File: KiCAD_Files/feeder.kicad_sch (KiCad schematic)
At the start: 8 parts

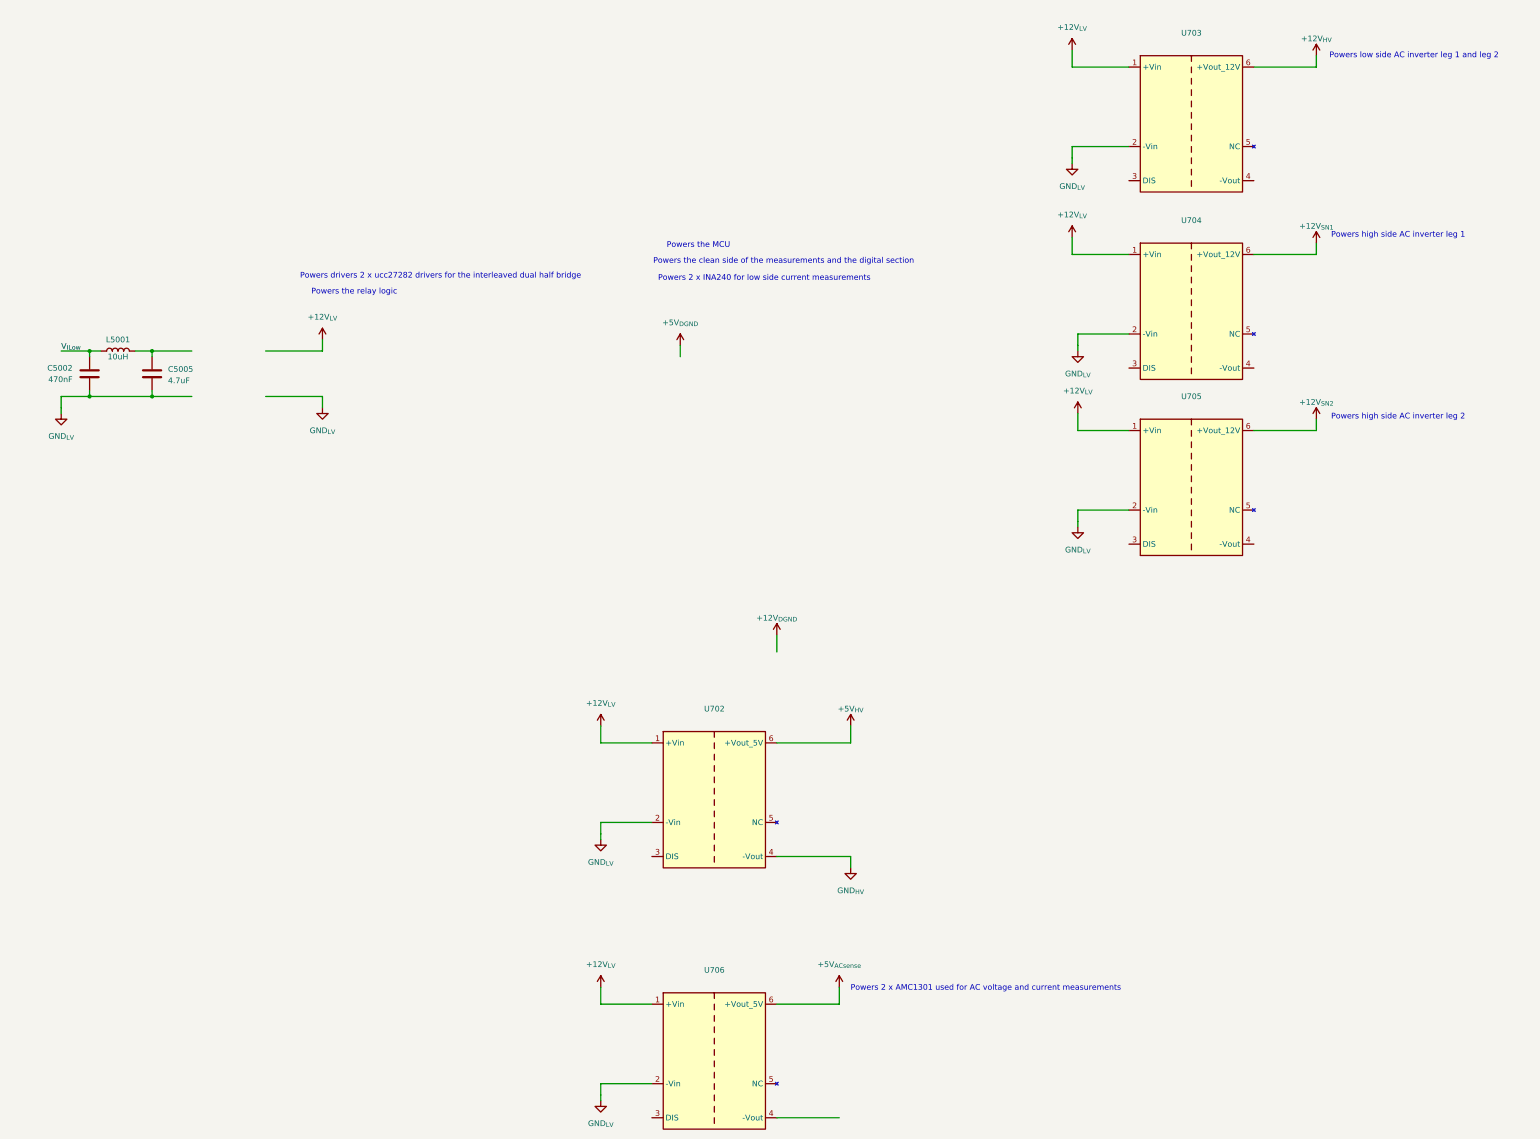
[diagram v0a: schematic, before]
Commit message: First routing pass complete.
Signed-off-by: Jean Alinei <jean.alinei@owntech.org>
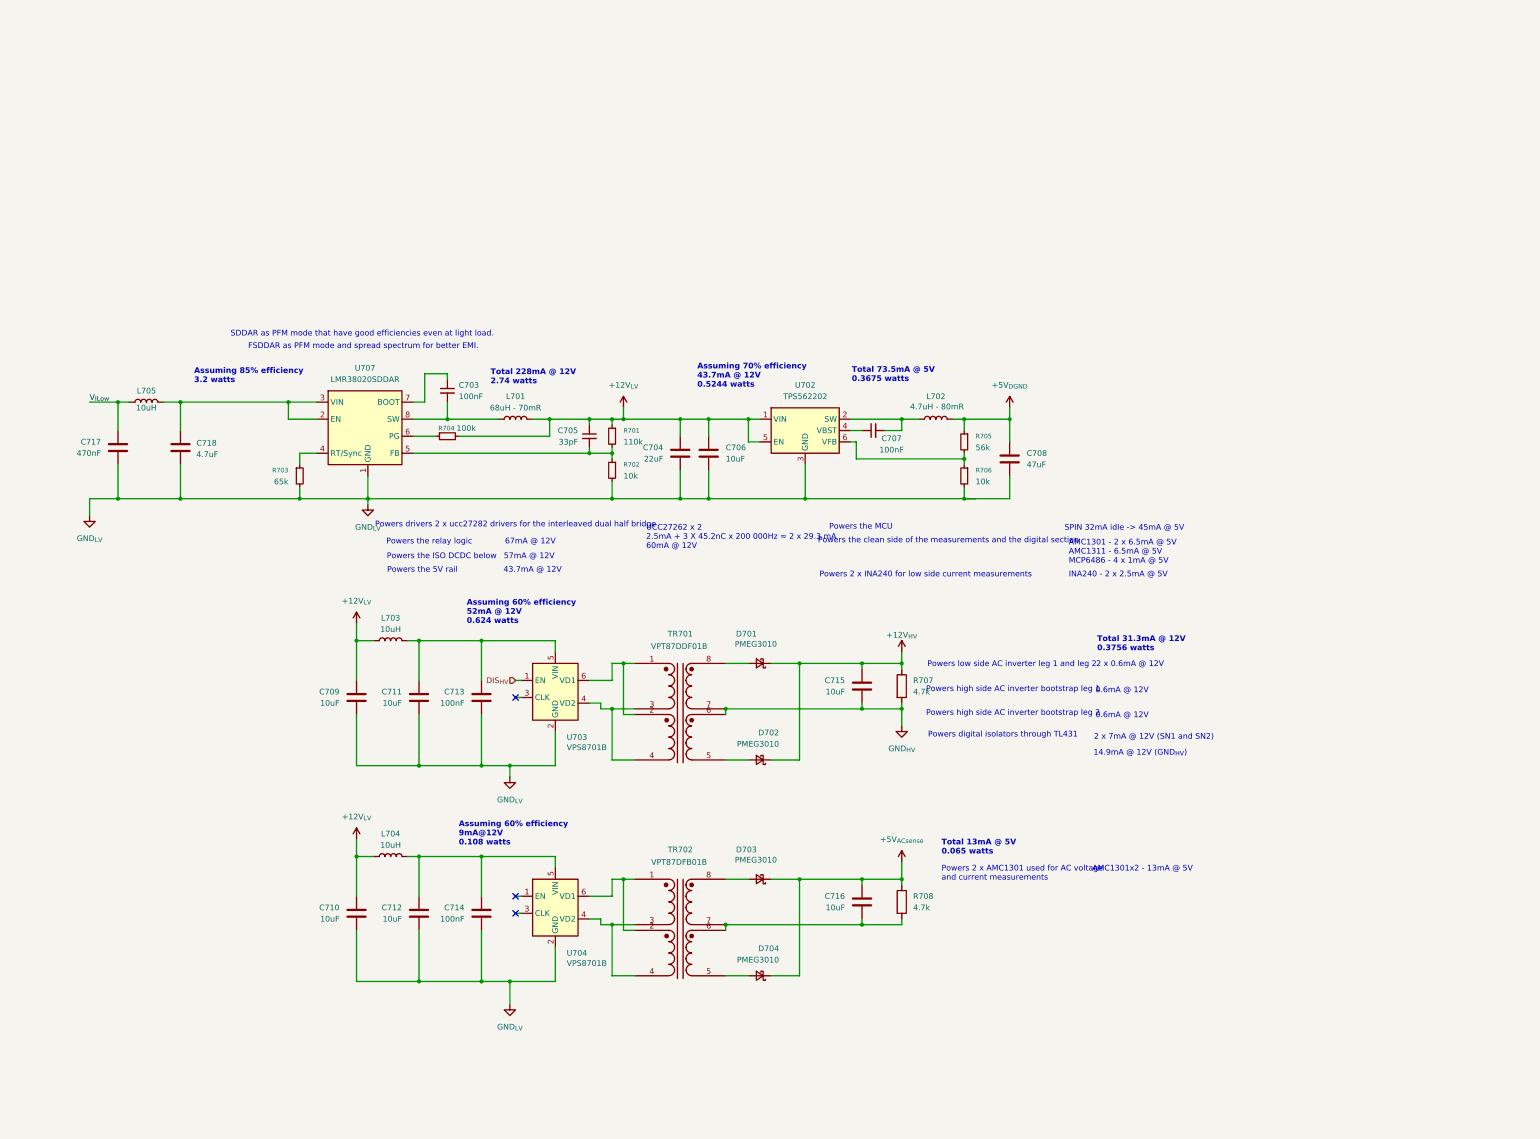
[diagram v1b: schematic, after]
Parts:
- removed U702, U706: ~, Footprints:Feeder_05_05_2, symbol Symbols:Isolated DCDC 5V -{gt} 5V
- removed U703, U704, U705: ~, Footprints:Feeder_12_12_2, symbol Symbols:Isolated DCDC 12V -{gt} 12V
- added C703, C707: 100nF, Capacitor_SMD:C_0805_2012Metric, symbol Device:C_Small
- added C704: 22uF, Capacitor_SMD:C_1210_3225Metric, symbol Device:C
- added C705: 33pF, Capacitor_SMD:C_0805_2012Metric, symbol Device:C_Small
- added C706, C709, C710, C711, C712, C715, C716: 10uF, Capacitor_SMD:C_0805_2012Metric, symbol Device:C
- added C708: 47uF, Capacitor_SMD:C_1206_3216Metric, symbol Device:C
- added C713, C714: 100nF, Capacitor_SMD:C_0603_1608Metric, symbol Device:C
- added D701, D702, D703, D704: PMEG3010, Diode_SMD:D_SOD-323F, symbol Device:D_Schottky_Small
- added L701: 68uH - 70mR, Inductor_SMD:L_12x12mm_H6mm, symbol Device:L
- added L702: 4.7uH - 80mR, Inductor_SMD:L_Cenker_CKCS4020, symbol Device:L
- added L703, L704: 10uH, Inductor_SMD:L_0805_2012Metric, symbol Device:L
- added R701: 110k, Footprints:R_0805_2012Metric, symbol Device:R_Small
- added R702, R706: 10k, Footprints:R_0805_2012Metric, symbol Device:R_Small
- added R703: 65k, Footprints:R_0805_2012Metric, symbol Device:R_Small
- added R704: 100k, Footprints:R_0805_2012Metric, symbol Device:R_Small
- added R705: 56k, Footprints:R_0805_2012Metric, symbol Device:R_Small
- added R707, R708: 4.7k, Resistor_SMD:R_0603_1608Metric, symbol Device:R
- added TR701: VPT87DDF01B, Footprints:VPT87BB-01B, symbol Symbols:Transformer_2P_2S
- added TR702: VPT87DFB01B, Footprints:VPT87BB-01B, symbol Symbols:Transformer_2P_2S
- added U702: TPS562202, Package_TO_SOT_SMD:SOT-563, symbol Regulator_Switching:TPS562202
- added U703, U704: VPS8701B, Package_TO_SOT_SMD:SOT-23-6, symbol Symbols:VPS8504B
- added U707: LMR38020SDDAR, Package_SO:Texas_HSOP-8-1EP_3.9x4.9mm_P1.27mm_ThermalVias, symbol Symbols:LMR38020
- renumbered C5002 to C717, C5005 to C718, L5001 to L705
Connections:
- net +12V_{HV}: now also C715.1, D701.1 (K), D702.1 (K), R707.1
- net +12V_{LV}: now also C704.1, C705.1, C706.1, C709.1, C710.1, L701.2, L703.1, L704.1, R701.1, R704.2, U702.1 (VIN), U702.5 (EN)
- net +5V_{ACsense}: now also C716.1, D703.1 (K), D704.1 (K), R708.1
- net +5V_{DGND}: now also C708.1, L702.2, R705.1
- net GND_{HV}: now also C715.2, R707.2, TR701.6 (SB), TR701.7 (SA)
- net GND_{LV}: now also C704.2, C706.2, C708.2, C709.2, C710.2, C711.2, C712.2, C713.2, C714.2, R702.2, R703.2, R706.2, U702.3 (GND), U703.2 (GND), U704.2 (GND), U707.1 (GND), U707.9 (GND)
- net at C718.1, L705.2: now also U707.2 (EN), U707.3 (VIN)
- new net: C716.2, R708.2, TR702.6 (SB), TR702.7 (SA)
- new net: C712.1, C714.1, L704.2, U704.5 (VIN)
- new net: D702.2 (A), TR701.5 (SA)
- new net: D704.2 (A), TR702.5 (SA)
- new net: C711.1, C713.1, L703.2, U703.5 (VIN)
- new net: C703.2, L701.1, U707.8 (SW)
- new net: R703.1, U707.4 (RT/Sync)
- new net: C705.2, R701.2, R702.1, U707.5 (FB)
- new net: R704.1, U707.6 (PG)
- new net: C703.1, U707.7 (BOOT)
- new net: TR701.1 (AA), TR701.2 (AA), U703.6 (VD1)
- new net: TR701.3 (AB), TR701.4 (AB), U703.4 (VD2)
- new net: D701.2 (A), TR701.8 (SB)
- new net: C707.2, L702.1, U702.2 (SW)
- new net: TR702.1 (AA), TR702.2 (AA), U704.6 (VD1)
- new net: TR702.3 (AB), TR702.4 (AB), U704.4 (VD2)
- new net: D703.2 (A), TR702.8 (SB)
- new net: R705.2, R706.1, U702.6 (VFB)
- new net: C707.1, U702.4 (VBST)
- new net DIS_{HV}: U703.1 (EN)
- no-connect marks 0 -> 3
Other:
- note added: "0.6mA @ 12V"
- note added: "14.9mA @ 12V (GND_{HV})"
- note added: "2 x 0.6mA @ 12V"
- note added: "2 x 7mA @ 12V (SN1 and SN2)"
- note added: "43.7mA @ 12V"
- note added: "57mA @ 12V"
- note added: "67mA @ 12V"
- note added: "AMC1301 - 2 x 6.5mA @ 5V AMC1311 - 6.5mA @ 5V MCP6486 - 4 x 1mA @ 5V"
- note added: "AMC1301x2 - 13mA @ 5V"
- note added: "Assuming 60% efficiency 52mA @ 12V 0.624 watts"
- note added: "Assuming 60% efficiency 9mA@12V 0.108 watts"
- note added: "Assuming 70% efficiency 43.7mA @ 12V 0.5244 watts"
- note added: "Assuming 85% efficiency 3.2 watts"
- note added: "FSDDAR as PFM mode and spread spectrum for better EMI."
- note added: "INA240 - 2 x 2.5mA @ 5V"
- note added: "Powers digital isolators through TL431"
- note added: "Powers high side AC inverter bootstrap leg 1"
- note added: "Powers high side AC inverter bootstrap leg 2"
- note added: "Powers the 5V rail"
- note added: "Powers the ISO DCDC below"
- note added: "SDDAR as PFM mode that have good efficiencies even at light load."
- note added: "SPIN 32mA idle -> 45mA @ 5V"
- note added: "Total 13mA @ 5V 0.065 watts"
- note added: "Total 228mA @ 12V 2.74 watts"
- note added: "Total 31.3mA @ 12V 0.3756 watts"
- note added: "Total 73.5mA @ 5V 0.3675 watts"
- note added: "UCC27262 x 2 2.5mA + 3 X 45.2nC x 200 000Hz ≈ 2 x 29.3 mA 60mA @ 12V"
- note removed: "Powers high side AC inverter leg 1"
- note removed: "Powers high side AC inverter leg 2"
- moved on the sheet: C717, C718, L705

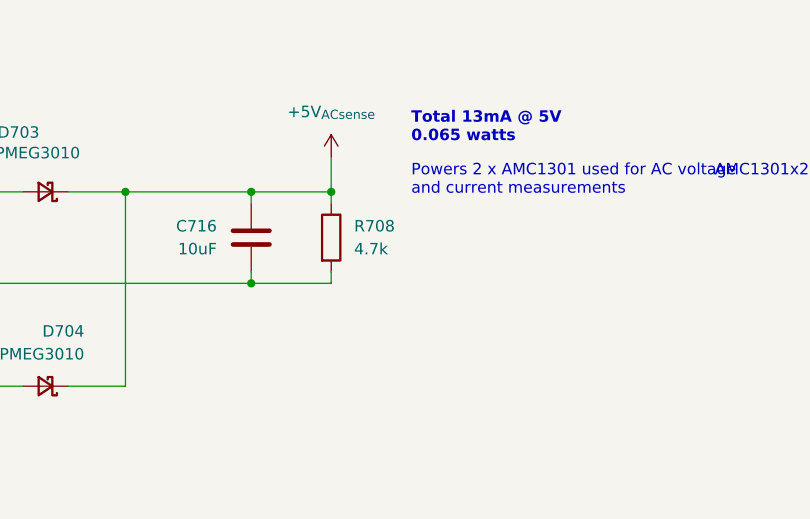
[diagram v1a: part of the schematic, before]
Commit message: Added missing tracks for sensors and relay. Fixed many routing issues.
Signed-off-by: Jean Alinei <jean.alinei@owntech.org>
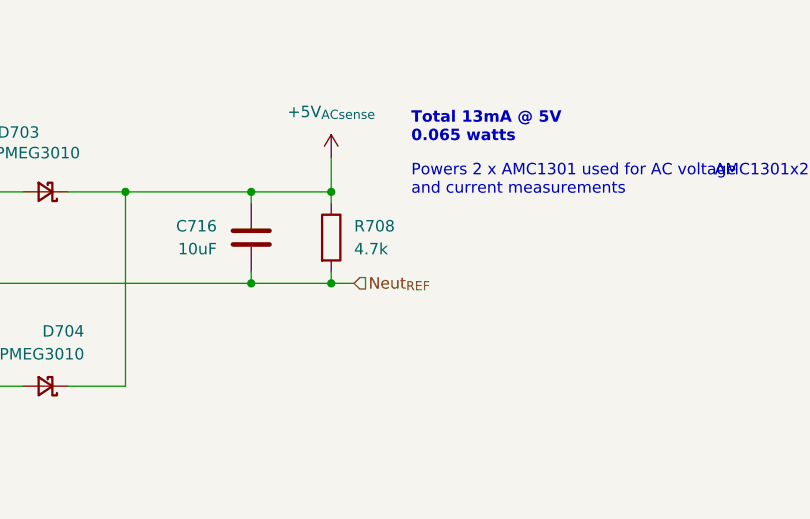
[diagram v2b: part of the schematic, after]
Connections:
- net Neut_{REF}: now reaches C716.2, R708.2, TR702.6 (SB), TR702.7 (SA)
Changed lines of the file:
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@@
+	)
+	(junction
+		(at 214.63 220.98)
+		(diameter 0)
+		(color 0 0 0 0)
 	)
 	(junction
@@
 		(pts
 			(xy 120.65 185.42) (xy 127 185.42)
+		)
+		(stroke
+			(width 0)
+			(type default)
+		)
+	)
+	(wire
+		(pts
+			(xy 214.63 220.98) (xy 217.17 220.98)
 		)
 		(stroke
@@
 		)
 	)
+	(hierarchical_label "Neut_{REF}"
+		(shape input)
+		(at 217.17 220.98 0)
+		(effects
+			(font
+				(size 1.27 1.27)
+			)
+			(justify left)
+		)
+	)
+	(rule_area
+		(polyline
+			(pts
+				(xy 26.67 247.65) (xy 165.1 247.65) (xy 165.1 149.86) (xy 278.13 149.86) (xy 278.13 85.09) (xy 26.67 85.09)
+			)
+			(stroke
+				(width 0)
+				(type dash)
+			)
+			(fill
+				(type none)
+			)
+		)
+	)
+	(netclass_flag ""
+		(length 2.54)
+		(shape round)
+		(at 46.99 247.65 0)
+		(fields_autoplaced yes)
+		(effects
+			(font
+				(size 1.27 1.27)
+			)
+			(justify left bottom)
+		)
+		(property "Netclass" "DGND"
+			(at 47.6885 245.11 0)
+			(effects
+				(font
+					(size 1.27 1.27)
+				)
+				(justify left)
+			)
+		)
+		(property "Component Class" ""
+			(at -322.58 166.37 0)
+			(effects
+				(font
+					(size 1.27 1.27)
+					(italic yes)
+				)
+			)
+		)
+	)

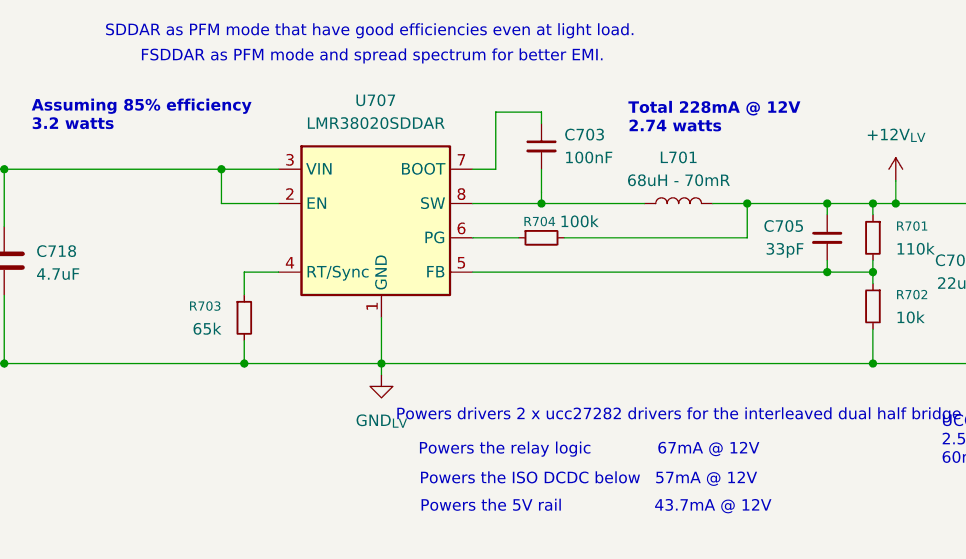
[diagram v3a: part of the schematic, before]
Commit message: Added passive references. Added ESD protection for MCU pins.
Signed-off-by: Jean Alinei <jean.alinei@owntech.org>
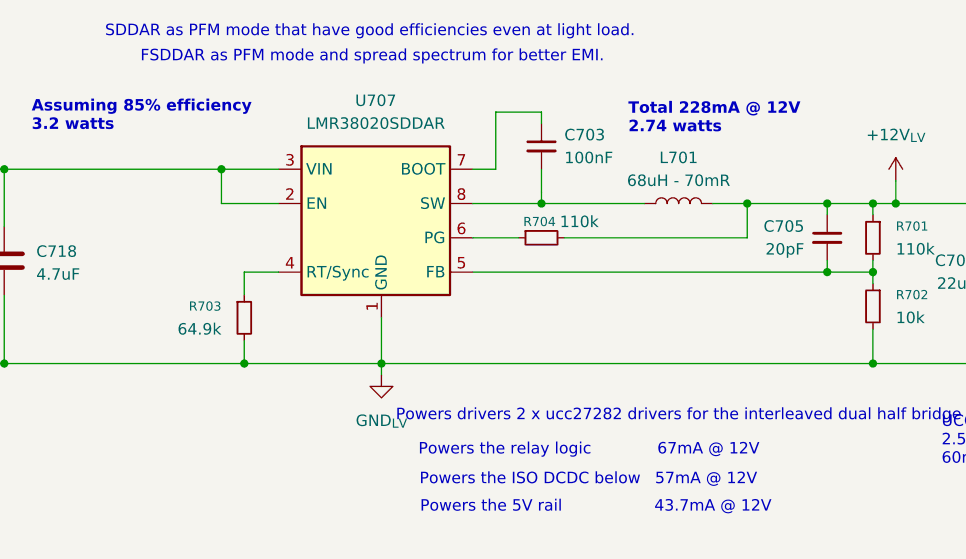
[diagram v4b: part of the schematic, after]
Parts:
- C703, C707: LCSC (none) -> C49678
- C704: LCSC (none) -> C309062
- C705: value 33pF -> 20pF; LCSC (none) -> C1798
- C706: LCSC (none) -> C440198
- C708: LCSC (none) -> C96123
- C717: Dielectric X7R -> (none); LCSC (none) -> C596323; Metal content BaTiO3 -> (none); Reserved1 541c32eba89ffcf7615ab170cc4034ba7c4f621972be10 -> (none); Subfunction +6V / DGND supply -> (none); manf# GRM21BR72A474KA73L -> (none)
- C718: Dielectric X7R -> (none); Functional Block Feeder -> (none); LCSC (none) -> C381466; Metal content BaTiO3 -> (none); Reserved1 0db098cf967df37918c59b0e08ade59c874a0accb68a991e -> (none); Subfunction +6V / DGND supply -> (none); Voltage_Rating 100V -> (none); manf# CL32B475KCVZNWE -> (none)
- D701, D702, D703, D704: LCSC C255586 -> C2937140
- L703, L704: LCSC (none) -> C88173
- L705: LCSC (none) -> C2047632; Reserved1 9caf66ac32bc3e6935764377581ec0eb3af5b0b6a22e -> (none); Subfunction +6V / DGND supply -> (none); manf# CBC3225T100M -> (none)
- R701: LCSC (none) -> C17422
- R702, R706: LCSC (none) -> C17414
- R703: value 65k -> 64.9k; LCSC (none) -> C17788
- R704: value 100k -> 110k; LCSC (none) -> C17422
- R705: LCSC (none) -> C17756
- TR701, TR702, U702, U707: Rotation Offset (none) -> 270
- U703, U704: Rotation Offset (none) -> 90
